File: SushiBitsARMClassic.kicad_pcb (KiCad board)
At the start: 2 copper layers, 68.6 x 53.3 mm, 77 parts, among them J1 JTAG, J2 SPI, J3 DC12V, J4 USB_B, J5 Conn_ARM_JTAG_SWD_10, M1 LPC2103, P1 CONN_01X01, P2 CONN_01X01, P3 CONN_01X01, P4 CONN_01X01, P5 Digital, P6 Power, P7 Digital, P8 Analog, SW1 RESET, U1 MAX811S, U2 LMV321, U3 TPS563200, U4 TPS563200, U5 LP2985-1.8, U6 STM32F042F4Px, U7 24LC512, Y1 32768, Y2 16M, Y3 16M

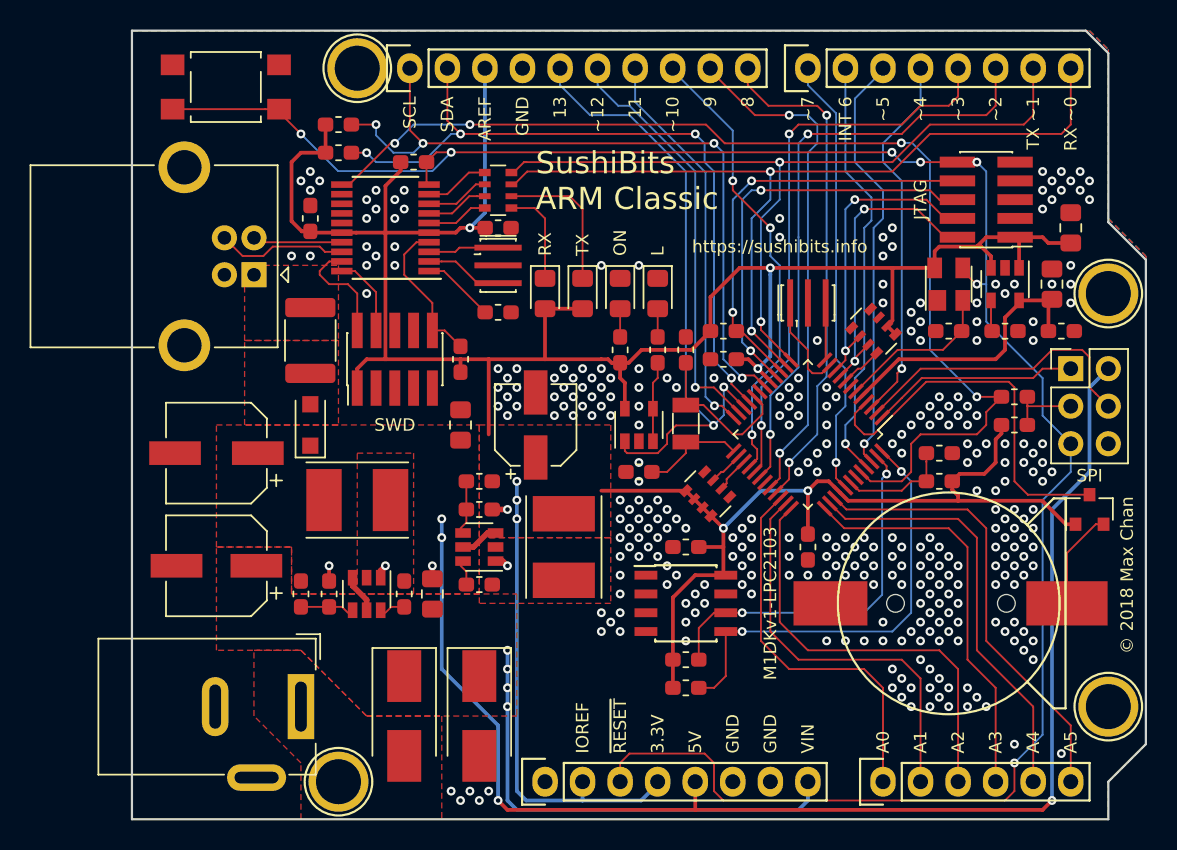
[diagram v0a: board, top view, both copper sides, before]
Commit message: Rework: improving power delivery
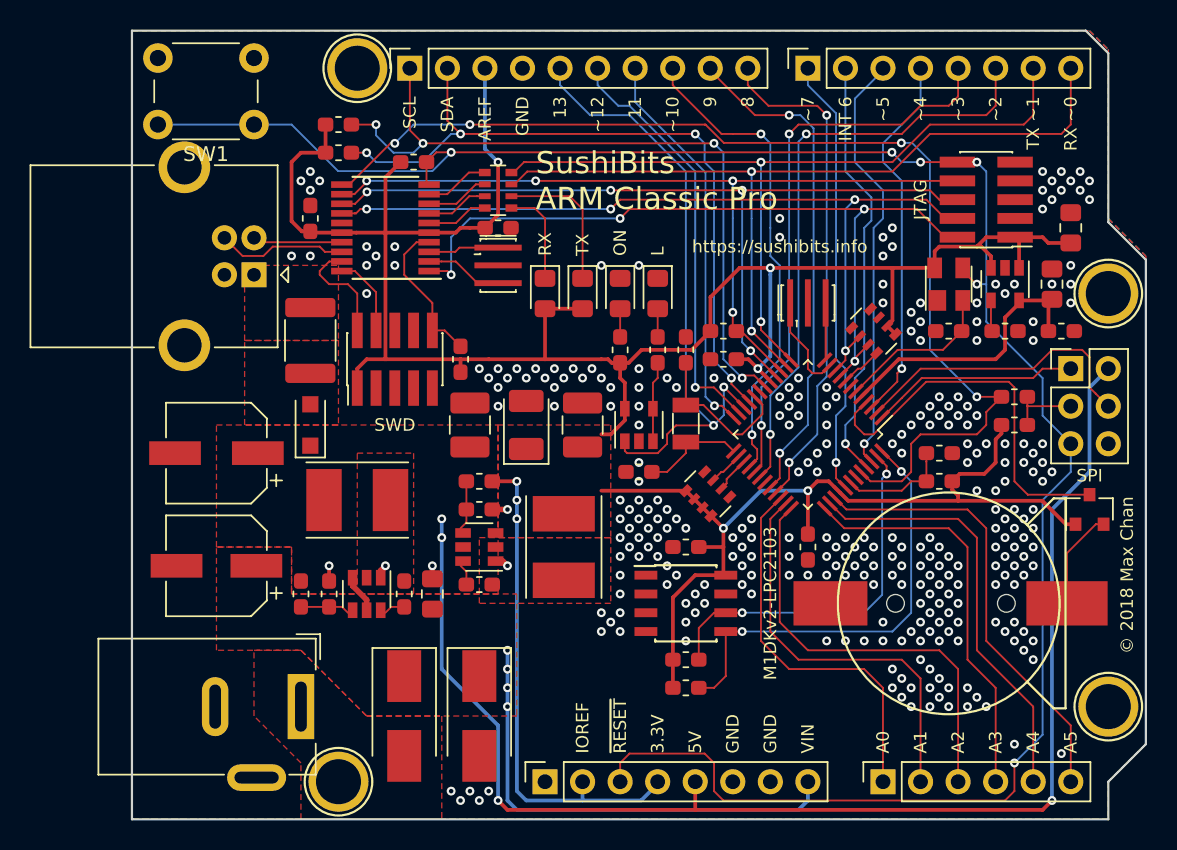
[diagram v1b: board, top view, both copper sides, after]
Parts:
- removed the C12 at (133.2, 99.7)
- removed the C13 at (138.3, 99.7)
- removed the P5 at (129.8, 75.6)
- removed the P6 at (138.9, 123.8)
- removed the P7 at (156.7, 75.6)
- removed the P8 at (161.8, 123.8)
- removed the R13 at (135.8, 92.1)
- added C10: 47µ, Capacitor_SMD:C_1210_3225Metric_Pad1.42x2.65mm_HandSolder, F.Cu at (133.9, 99.7)
- added C17: 220µ, Capacitor_Tantalum_SMD:CP_EIA-3528-12_Kemet-T_Pad1.50x2.35mm_HandSolder, F.Cu at (137.7, 99.7)
- added C18: 47u, Capacitor_SMD:C_1210_3225Metric_Pad1.42x2.65mm_HandSolder, F.Cu at (141.5, 99.7)
- added P1: Power, Connector_PinSocket_2.54mm:PinSocket_1x08_P2.54mm_Vertical, F.Cu at (138.9, 123.8)
- added P2: Analog, Connector_PinSocket_2.54mm:PinSocket_1x06_P2.54mm_Vertical, F.Cu at (161.8, 123.8)
- added P3: Digital, Connector_PinSocket_2.54mm:PinSocket_1x10_P2.54mm_Vertical, F.Cu at (129.8, 75.6)
- added P4: Digital, Connector_PinSocket_2.54mm:PinSocket_1x08_P2.54mm_Vertical, F.Cu at (156.7, 75.6)
- SW1: footprint Button_Switch_SMD:SW_SPST_TL3305A -> Button_Switch_THT:SW_PUSH_6mm
- moved SW1 3.18 mm to (119.3, 79.4)
- renumbered C14 to C11, C15 to C12, C7 to C13, C11 to C14, C16 to C15, C10 to C16, C17 to C19, C18 to C20, C19 to C5, C5 to C6, C6 to C7, D6 to D4, D4 to D5, D5 to D6, J2 to J1, J1 to J2, P1 to P5, P2 to P6, P3 to P7, P4 to P8, R3 to R10, R8 to R11, R10 to R12, R7 to R13, R9 to R14, R11 to R15, R12 to R16, R14 to R3, R15 to R4, R6 to R5, R16 to R6, R5 to R7, R17 to R8, R4 to R9, U7 to U2, U2 to U3, U3 to U4, U4 to U5, U5 to U6, U6 to U7
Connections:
- U7 pad 1: Net-(R13-Pad1) -> /TMS
- U7 pad 12: (no net) -> /TDI
- U7 pad 13: (no net) -> /TDO
- U7 pad 14: (no net) -> /TCK
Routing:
- net /TCK: track 21.0 -> 56.1 mm, vias 2 -> 4
- net /TMS: track 20.5 -> 53.4 mm, vias 2 -> 4
- net /TDO: track 27.9 -> 55.8 mm, vias 2 -> 4
- net /TDI: track 28.8 -> 56.4 mm, vias 2 -> 4
- net Net-(R13-Pad1): track 4.95 -> 0.00 mm
- net +5V: track 93.4 -> 91.3 mm
- net /10: track 31.1 -> 32.8 mm, vias 3 -> 2
- net /0(RX): track 57.9 -> 57.4 mm
- net /1(TX): track 55.0 -> 54.5 mm
- net /9: track 34.8 -> 34.3 mm
- net /Reset: track 140.4 -> 140.8 mm, vias 7 -> 6
- net GND: vias 320 -> 301
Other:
- board text added: "M1DKv2-LPC2103"
- board text added: "SushiBits ARM Classic Pro"
- board text removed: "M1DKv1-LPC2103"
- board text removed: "SushiBits ARM Classic"
